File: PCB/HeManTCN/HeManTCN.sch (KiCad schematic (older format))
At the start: 110 parts, among them J101 VBATG, J102 VBAT+, J103 Micro_SD_Card, J104 Conn_02x03_Odd_Even, J105 Conn_02x02_Odd_Even, J106 Conn_02x05_Odd_Even, J107 Conn_02x12_Odd_Even, J108 Conn_02x12_Odd_Even, J109 Conn_02x05_Odd_Even, J110 Conn_02x12_Odd_Even, J111 USB_B, J112 USB_B, J113 73725-0110BLF, J114 Screw_Terminal_01x06, J115 RJ45_Amphenol_RJMG1BD3B8K1ANR, J116 Screw_Terminal_01x02, SW101 RESET, SW102 PC13, U101 STM32H743VITx, U102 MVBC02D, U103 S25FL127SABMFI101, U104 STM32F042F6Px, U105 TCAN332, U106 ISL83483, U107 USBLC6-2SC6, U108 KSZ8081RNA, U109 USBLC6-2SC6, U110 USBLC6-2SC6, U111 MIC2005A, U112 AP63203, Y101 8MHz, Y102 32.768KHz, Y103 25MHz

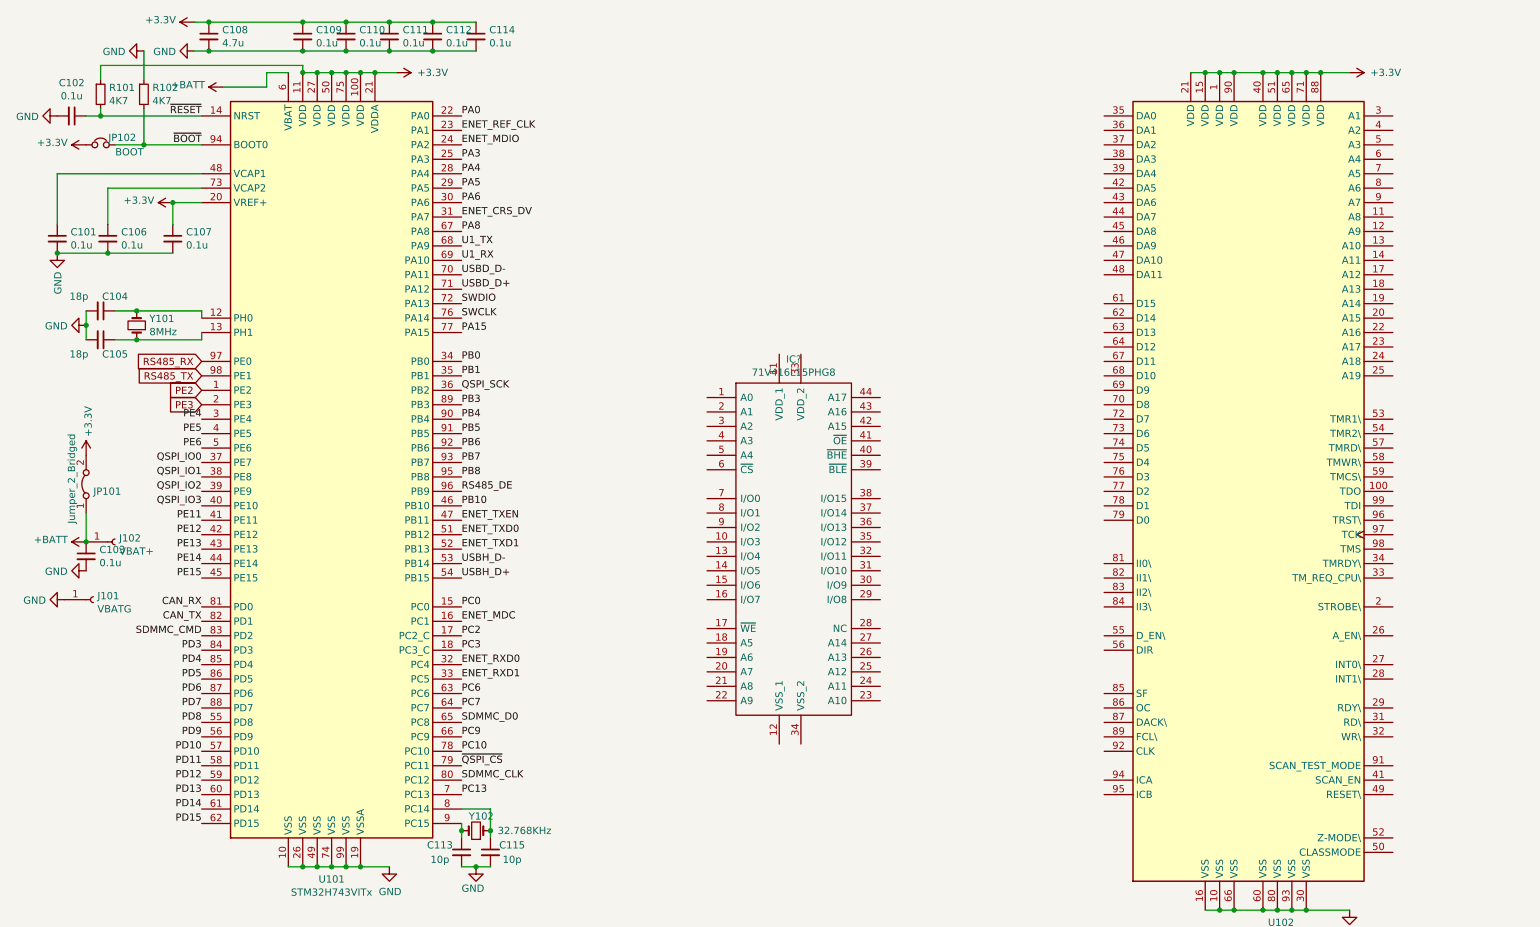
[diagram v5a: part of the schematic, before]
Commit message: Datasheet Memoria y conexiones
Agrege a DOCs el PDF de la memoria y ya hay varias conexiones del Esquematico realizadas.
MD (Master Data)
MA (Master Access)
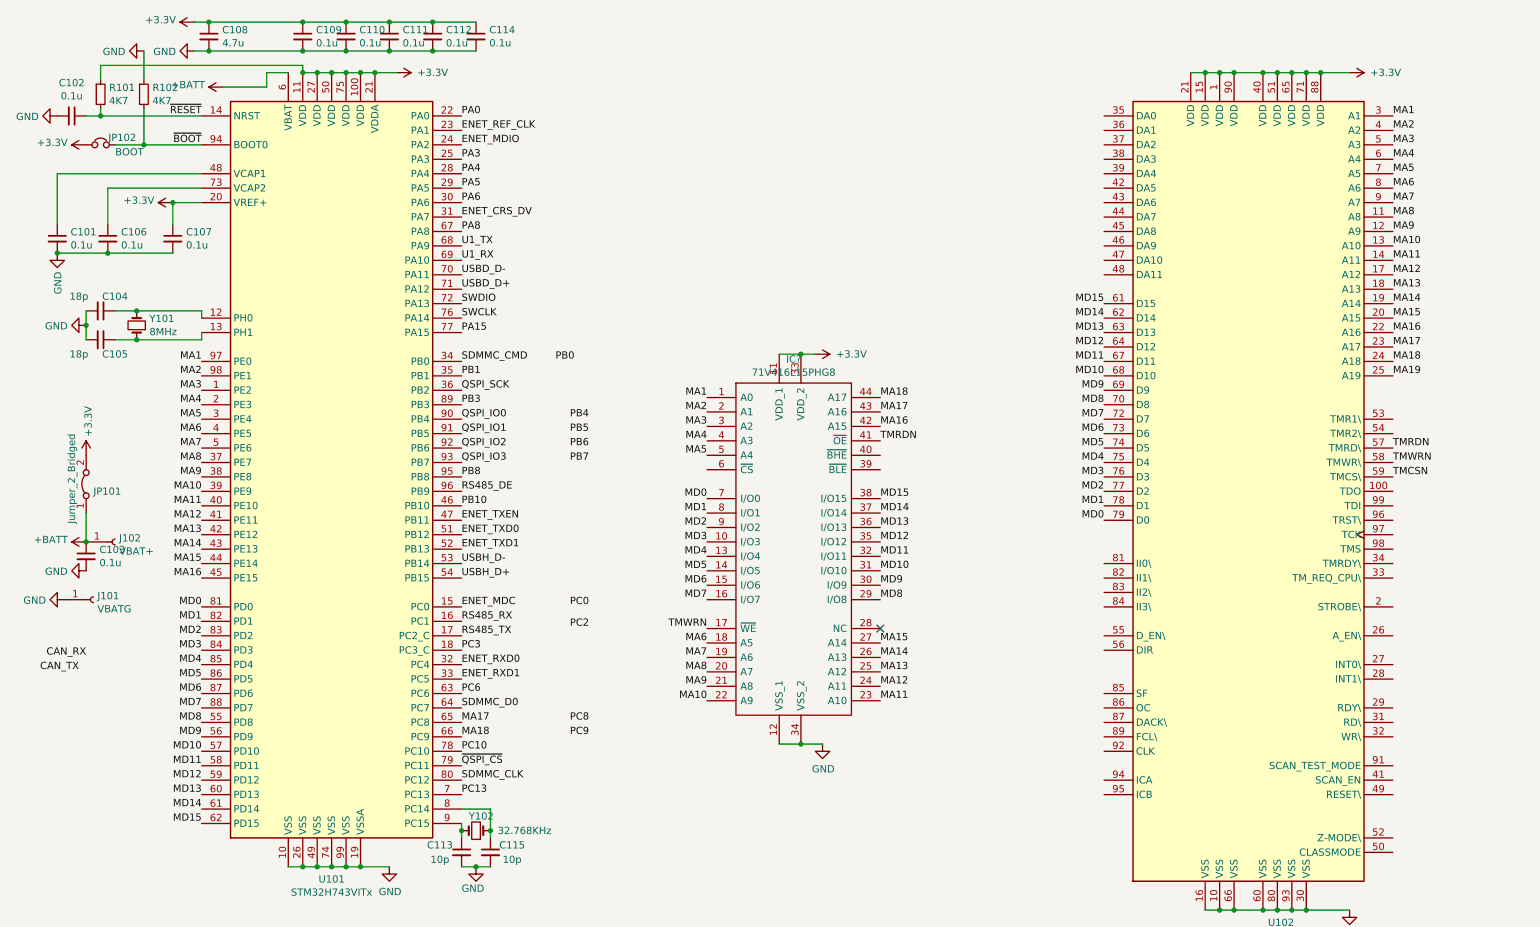
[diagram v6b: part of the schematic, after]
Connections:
- net +3V3: now also IC?.11 (VDD_1), IC?.33 (VDD_2)
- net CAN_RX: no longer U101.81 (PD0)
- net CAN_TX: no longer U101.82 (PD1)
- net ENET_MDC: now also U101.15 (PC0); no longer U101.16 (PC1)
- net GND: now also IC?.12 (VSS_1), IC?.34 (VSS_2)
- net PB0: no longer U101.34 (PB0)
- net PB4: no longer U101.90 (PB4)
- net PB5: no longer U101.91 (PB5)
- net PB6: no longer U101.92 (PB6)
- net PB7: no longer U101.93 (PB7)
- net PC0: no longer U101.15 (PC0)
- net PC2: no longer U101.17 (PC2_C)
- net PC7: no longer U101.64 (PC7)
- net PC9: no longer U101.66 (PC9)
- net PD10: no longer U101.57 (PD10)
- net PD11: no longer U101.58 (PD11)
- net PD12: no longer U101.59 (PD12)
- net PD13: no longer U101.60 (PD13)
- net PD14: no longer U101.61 (PD14)
- net PD15: no longer U101.62 (PD15)
- net PD3: no longer U101.84 (PD3)
- net PD4: no longer U101.85 (PD4)
- net PD5: no longer U101.86 (PD5)
- net PD6: no longer U101.87 (PD6)
- net PD7: no longer U101.88 (PD7)
- net PD8: no longer U101.55 (PD8)
- net PD9: no longer U101.56 (PD9)
- net PE11: no longer U101.41 (PE11)
- net PE12: no longer U101.42 (PE12)
- net PE13: no longer U101.43 (PE13)
- net PE14: no longer U101.44 (PE14)
- net PE15: no longer U101.45 (PE15)
- net PE2: no longer U101.1 (PE2)
- net PE3: no longer U101.2 (PE3)
- net PE4: no longer U101.3 (PE4)
- net PE5: no longer U101.4 (PE5)
- net PE6: no longer U101.5 (PE6)
- net QSPI_IO0: now also U101.90 (PB4); no longer U101.37 (PE7)
- net QSPI_IO1: now also U101.91 (PB5); no longer U101.38 (PE8)
- net QSPI_IO2: now also U101.92 (PB6); no longer U101.39 (PE9)
- net QSPI_IO3: now also U101.93 (PB7); no longer U101.40 (PE10)
- net RS485_RX: now also U101.16 (PC1); no longer U101.97 (PE0)
- net RS485_TX: now also U101.17 (PC2_C); no longer U101.98 (PE1)
- net SDMMC_CMD: now also U101.34 (PB0); no longer U101.83 (PD2)
- net SDMMC_D0: now also U101.64 (PC7); no longer U101.65 (PC8)
- net MA8: now reaches U102.11 (A8)
- net MA8: now also IC?.20 (A7), U101.37 (PE7)
- net MA9: now reaches U102.12 (A9)
- net MA9: now also IC?.21 (A8), U101.38 (PE8)
- net MA10: now reaches U102.13 (A10)
- net MA10: now also IC?.22 (A9), U101.39 (PE9)
- net MA11: now reaches U102.14 (A11)
- net MA11: now also IC?.23 (A10), U101.40 (PE10)
- net MA12: now reaches U102.17 (A12)
- net MA12: now also IC?.24 (A11), U101.41 (PE11)
- net MA13: now reaches U102.18 (A13)
- net MA13: now also IC?.25 (A12), U101.42 (PE12)
- net MA14: now reaches U102.19 (A14)
- net MA14: now also IC?.26 (A13), U101.43 (PE13)
- net MA15: now reaches U102.20 (A15)
- net MA15: now also IC?.27 (A14), U101.44 (PE14)
- net MA16: now reaches U102.22 (A16)
- net MA16: now also IC?.42 (A15), U101.45 (PE15)
- net MA17: now reaches U102.23 (A17)
- net MA17: now also IC?.43 (A16), U101.65 (PC8)
- net MA18: now reaches U102.24 (A18)
- net MA18: now also IC?.44 (A17), U101.66 (PC9)
- net MA19: now reaches U102.25 (A19)
- net MA1: now reaches U102.3 (A1)
- net MA1: now also IC?.1 (A0), U101.97 (PE0)
- net MA2: now reaches U102.4 (A2)
- net MA2: now also IC?.2 (A1), U101.98 (PE1)
- net MA3: now reaches U102.5 (A3)
- net MA3: now also IC?.3 (A2), U101.1 (PE2)
- net TMRDN: now reaches U102.57 (TMRD\)
- net TMRDN: now also IC?.41 (~OE)
- net TMWRN: now reaches U102.58 (TMWR\)
- net TMWRN: now also IC?.17 (~WE)
- net TMCSN: now reaches U102.59 (TMCS\)
- net MA4: now reaches U102.6 (A4)
- net MA4: now also IC?.4 (A3), U101.2 (PE3)
- net MD15: now reaches U102.61 (D15)
- net MD15: now also IC?.38 (I/O15), U101.62 (PD15)
- net MD14: now reaches U102.62 (D14)
- net MD14: now also IC?.37 (I/O14), U101.61 (PD14)
- net MD13: now reaches U102.63 (D13)
- net MD13: now also IC?.36 (I/O13), U101.60 (PD13)
- net MD12: now reaches U102.64 (D12)
- net MD12: now also IC?.35 (I/O12), U101.59 (PD12)
- net MD11: now reaches U102.67 (D11)
- net MD11: now also IC?.32 (I/O11), U101.58 (PD11)
- net MD10: now reaches U102.68 (D10)
- net MD10: now also IC?.31 (I/O10), U101.57 (PD10)
- net MD9: now reaches U102.69 (D9)
- net MD9: now also IC?.30 (I/O9), U101.56 (PD9)
- net MA5: now reaches U102.7 (A5)
- net MA5: now also IC?.5 (A4), U101.3 (PE4)
- net MD8: now reaches U102.70 (D8)
- net MD8: now also IC?.29 (I/O8), U101.55 (PD8)
- net MD7: now reaches U102.72 (D7)
- net MD7: now also IC?.16 (I/O7), U101.88 (PD7)
- net MD6: now reaches U102.73 (D6)
- net MD6: now also IC?.15 (I/O6), U101.87 (PD6)
- net MD5: now reaches U102.74 (D5)
- net MD5: now also IC?.14 (I/O5), U101.86 (PD5)
- net MD4: now reaches U102.75 (D4)
- net MD4: now also IC?.13 (I/O4), U101.85 (PD4)
- net MD3: now reaches U102.76 (D3)
- net MD3: now also IC?.10 (I/O3), U101.84 (PD3)
- net MD2: now reaches U102.77 (D2)
- net MD2: now also IC?.9 (I/O2), U101.83 (PD2)
- net MD1: now reaches U102.78 (D1)
- net MD1: now also IC?.8 (I/O1), U101.82 (PD1)
- net MD0: now reaches U102.79 (D0)
- net MD0: now also IC?.7 (I/O0), U101.81 (PD0)
- net MA6: now reaches U102.8 (A6)
- net MA6: now also IC?.18 (A5), U101.4 (PE5)
- net MA7: now reaches U102.9 (A7)
- net MA7: now also IC?.19 (A6), U101.5 (PE6)
- no-connect marks 8 -> 9

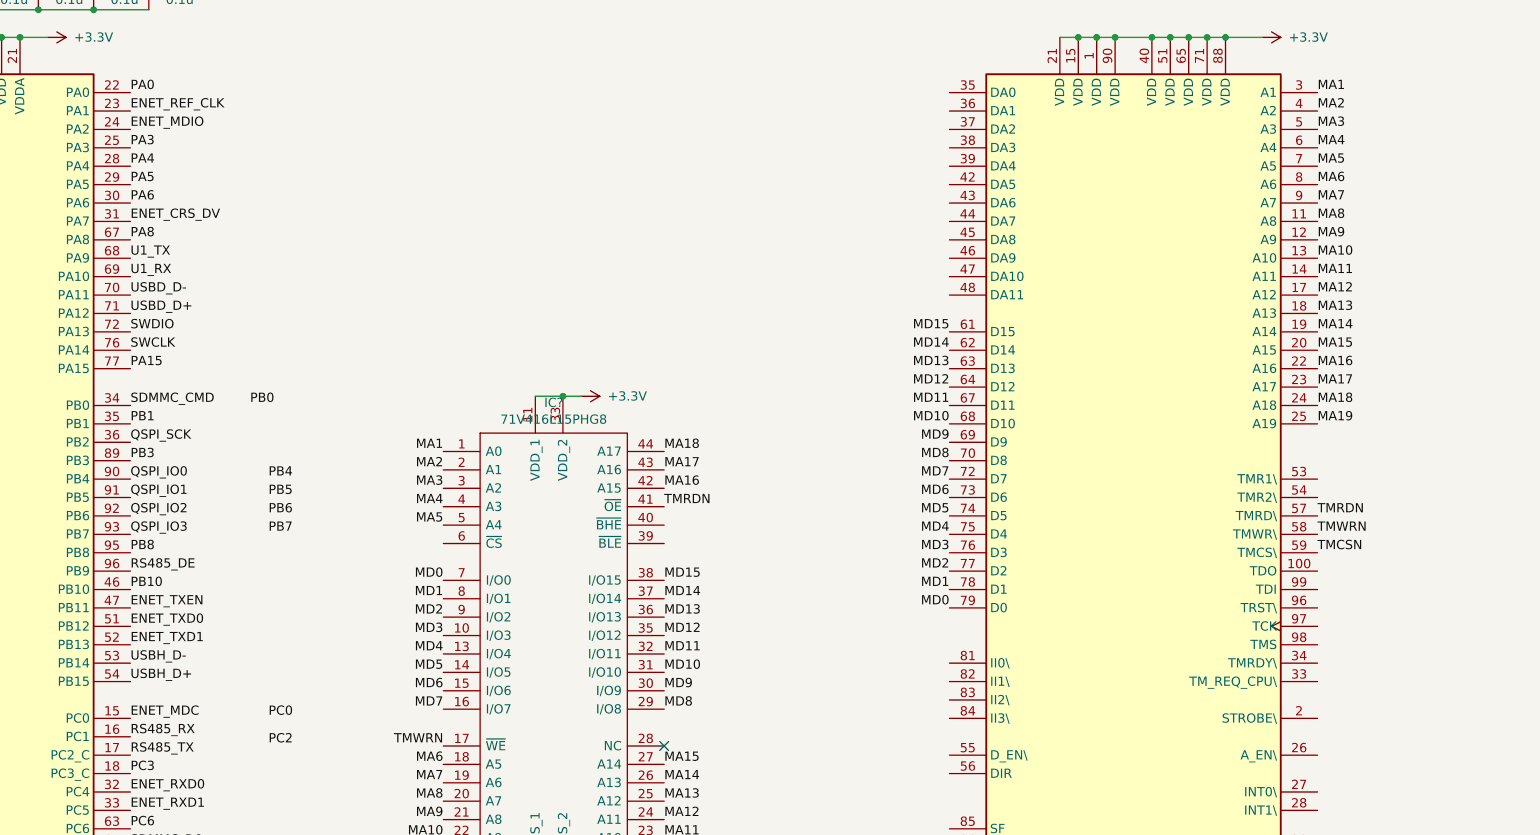
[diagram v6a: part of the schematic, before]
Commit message: DOCS y Ruteos basicos.
Separe en carpetas en DOCS y acomode parcialmente los pines del MVBC-02D que estan invertidos en la libreria.
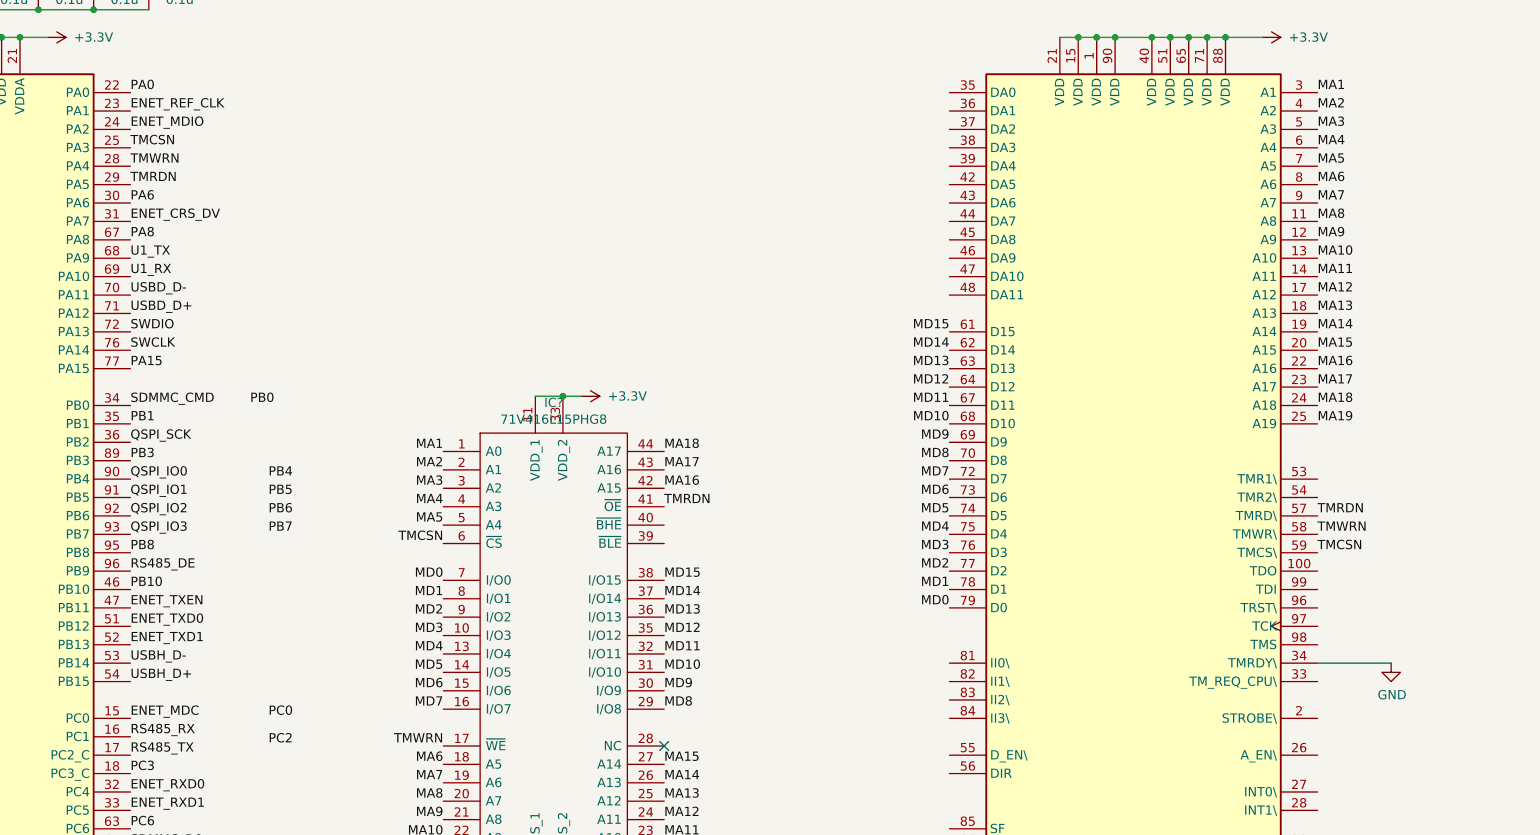
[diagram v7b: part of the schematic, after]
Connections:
- net GND: now also U102.34 (TMRDY\)
- net PA3: no longer U101.25 (PA3)
- net PA4: no longer U101.28 (PA4)
- net PA5: no longer U101.29 (PA5)
- net TMCSN: now also IC?.6 (~CS), U101.25 (PA3)
- net TMRDN: now also U101.29 (PA5)
- net TMWRN: now also U101.28 (PA4)
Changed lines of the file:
@@
 PA0
 Text Label 4750 2850 0    50   ~ 0
-PA3
+TMCSN
 Text Label 4750 2950 0    50   ~ 0
-PA4
+TMWRN
 Text Label 4750 3050 0    50   ~ 0
-PA5
+TMRDN
 Text Label 4750 3150 0    50   ~ 0
 PA6
@@
 Text Label 11200 5050 0    50   ~ 0
 TMCSN
+Text Label 6450 5000 2    50   ~ 0
+TMCSN
+$Comp
+L power:GND #PWR?
+U 1 1 5E02C64F
+P 11600 5650
+AR Path="/5E02C64F" Ref="#PWR?"  Part="1"
+AR Path="/5DA2C15A/5E02C64F" Ref="#PWR?"  Part="1"
+F 0 "#PWR?" H 11600 5400 50  0001 C CNN
+F 1 "GND" H 11605 5477 50  0000 C CNN
+F 2 "" H 11600 5650 50  0001 C CNN
+F 3 "" H 11600 5650 50  0001 C CNN
+	1    11600 5650
+	1    0    0    -1
+$EndComp
+Wire Wire Line
+	11200 5650 11600 5650
 $EndSCHEMATC
